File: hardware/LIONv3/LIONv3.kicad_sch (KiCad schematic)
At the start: 39 parts, among them SW1 RESET, SW2 BOOT, U1 TCAN3414DR, U14 HC-1_25-2PWT, U15 HC-1_25-2PWT, U19 HC-1_25-2PWT, U2 TYPE-C_16PIN_2MD(073), U21 USBLC6-2SC6, U3 ESP32-C6-MINI-1-N4, U4 TMP112AIDRLR, U9 HC-1_25-2PWT

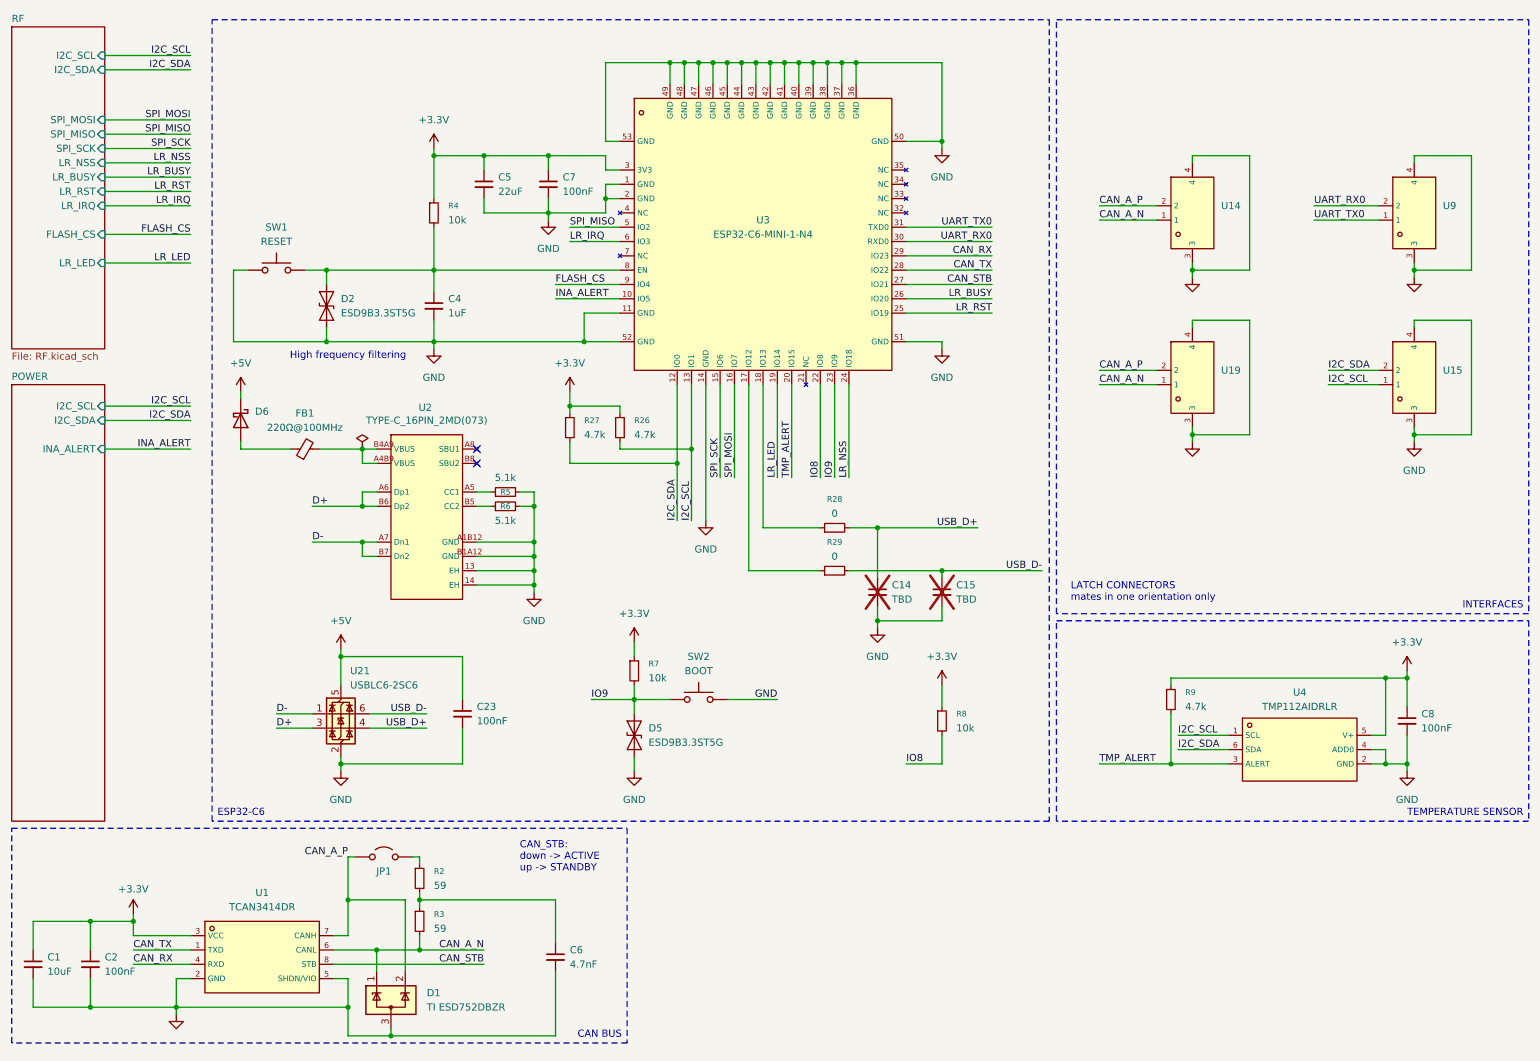
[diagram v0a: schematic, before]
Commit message: feat(hardware): change SPI terminology (new OSHWA naming conventions)
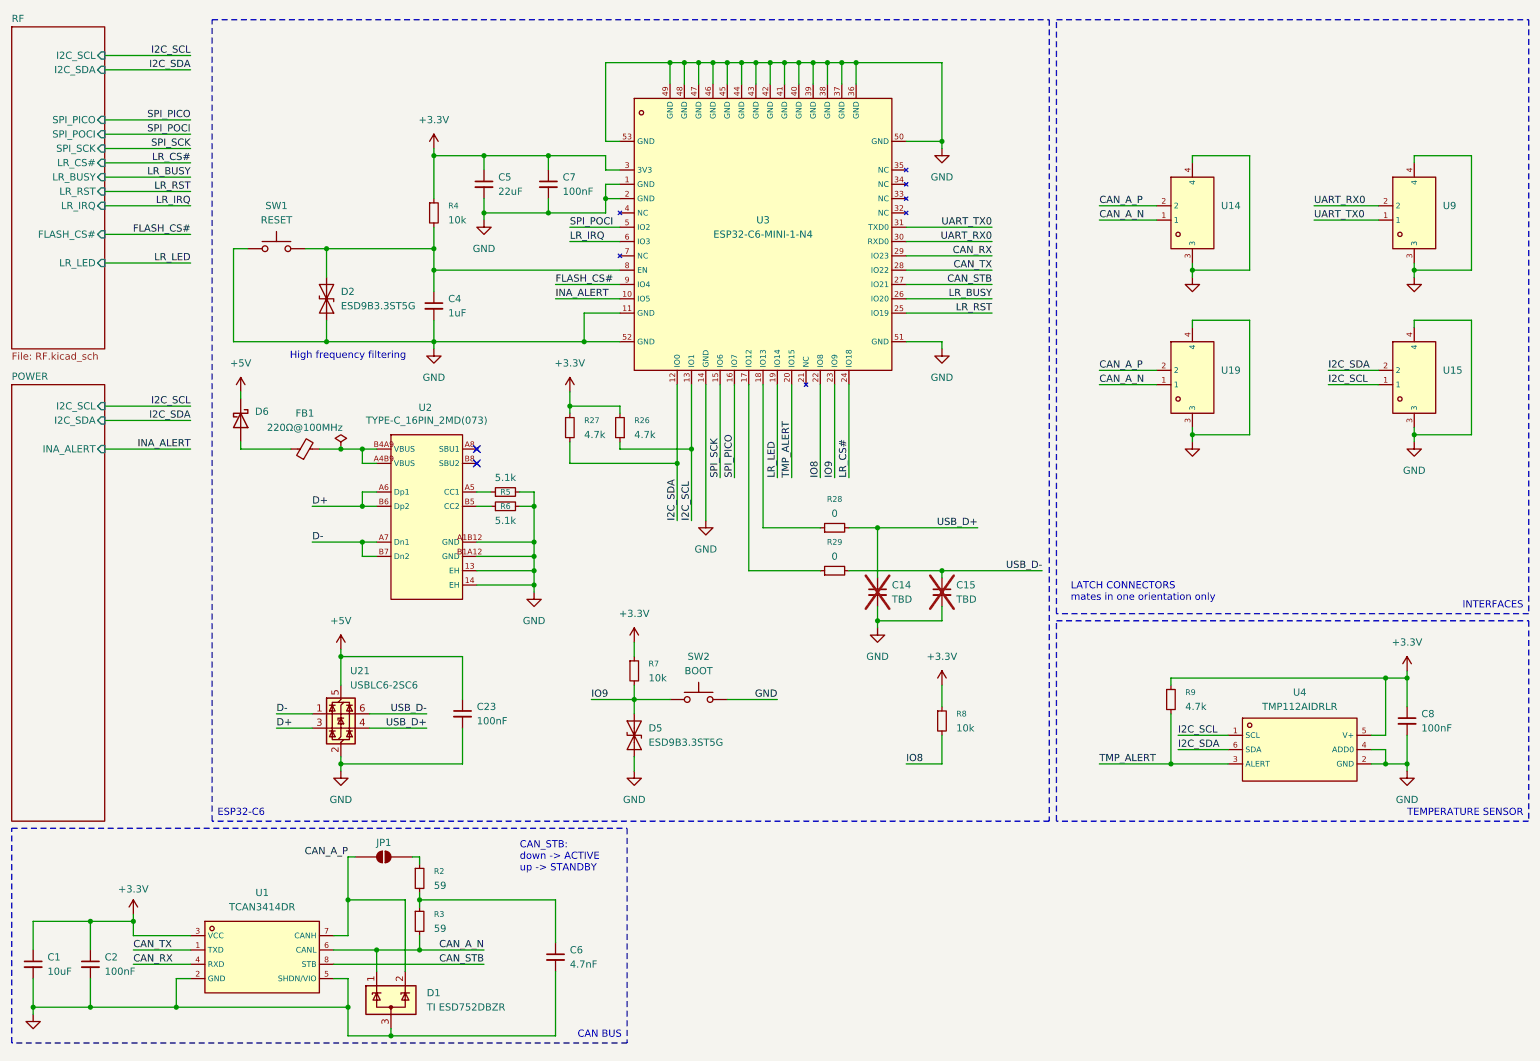
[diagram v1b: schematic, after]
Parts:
- removed JP1: Jumper_2_Open, Jumper:SolderJumper-2_P1.3mm_Open_TrianglePad1.0x1.5mm, symbol Jumper:Jumper_2_Open
- added JP1: SolderJumper_2_Open, Jumper:SolderJumper-2_P1.3mm_Open_TrianglePad1.0x1.5mm, symbol Jumper:SolderJumper_2_Open
- FB1: footprint Capacitor_SMD:C_0805_2012Metric -> Inductor_SMD:L_0805_2012Metric
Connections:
- net CAN_A_P: now also JP1.1 (A)
- net at R2.1: now also JP1.2 (B)
- net FLASH_CS renamed FLASH_CS#
- net LR_NSS renamed LR_CS#
- net SPI_MISO renamed SPI_POCI
- net SPI_MOSI renamed SPI_PICO
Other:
- sheet RF ports: added FLASH_CS#, LR_CS#, SPI_PICO, SPI_POCI; removed FLASH_CS, LR_NSS, SPI_MISO, SPI_MOSI
- moved on the sheet: D2, SW1

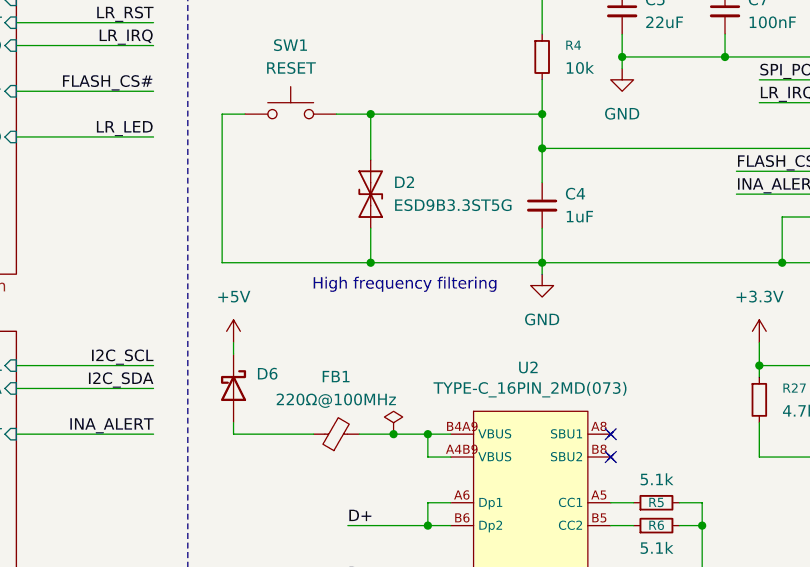
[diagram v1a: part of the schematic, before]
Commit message: feat(hardware): annotate schematic with I2C addresses
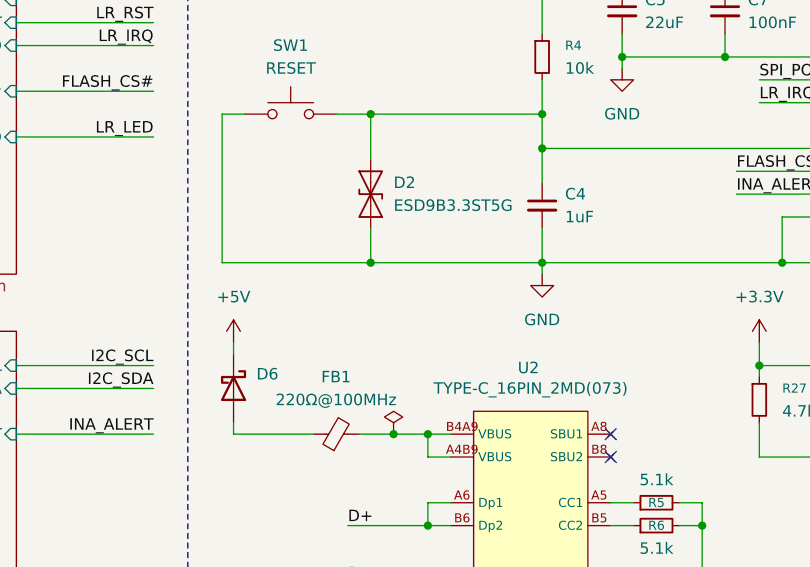
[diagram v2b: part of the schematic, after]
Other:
- note removed: "High frequency filtering"
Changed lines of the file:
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@@
 		(comment 3 "2026-08-12")
-	)
-	(text "High frequency filtering"
-		(exclude_from_sim no)
-		(at 73.66 73.66 0)
-		(effects
-			(font
-				(size 1.27 1.27)
-			)
-		)
 	)
 	(text "LATCH CONNECTORS\nmates in one orientation only"

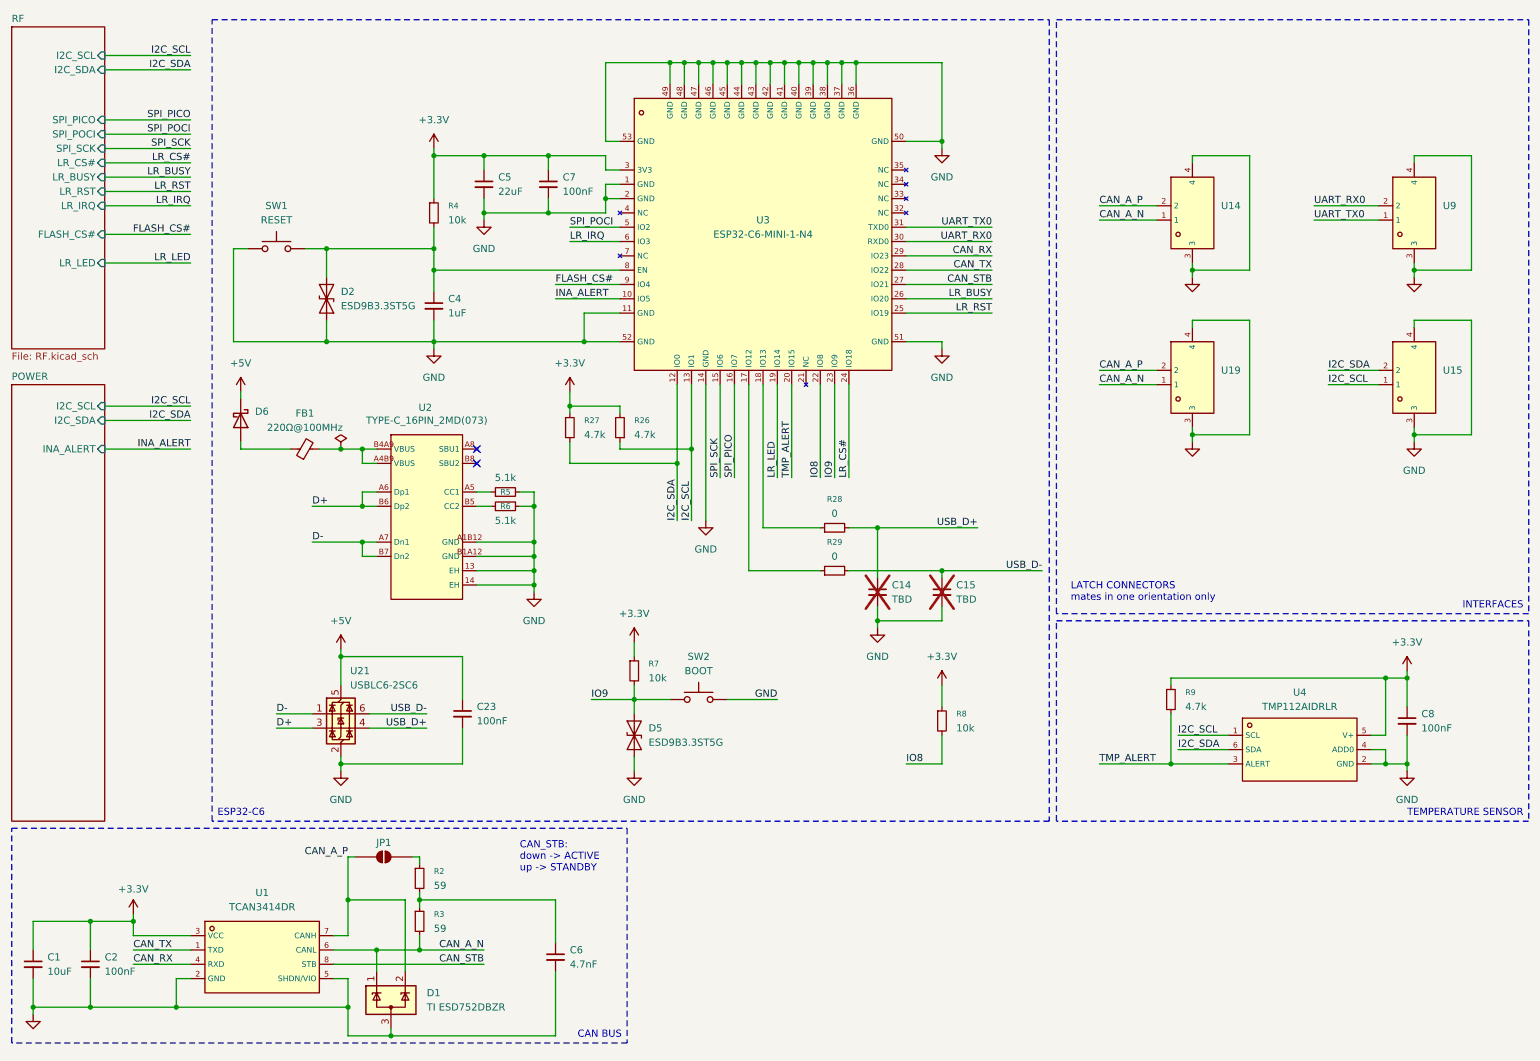
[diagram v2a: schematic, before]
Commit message: fix(hardware): fix CANbus split termination
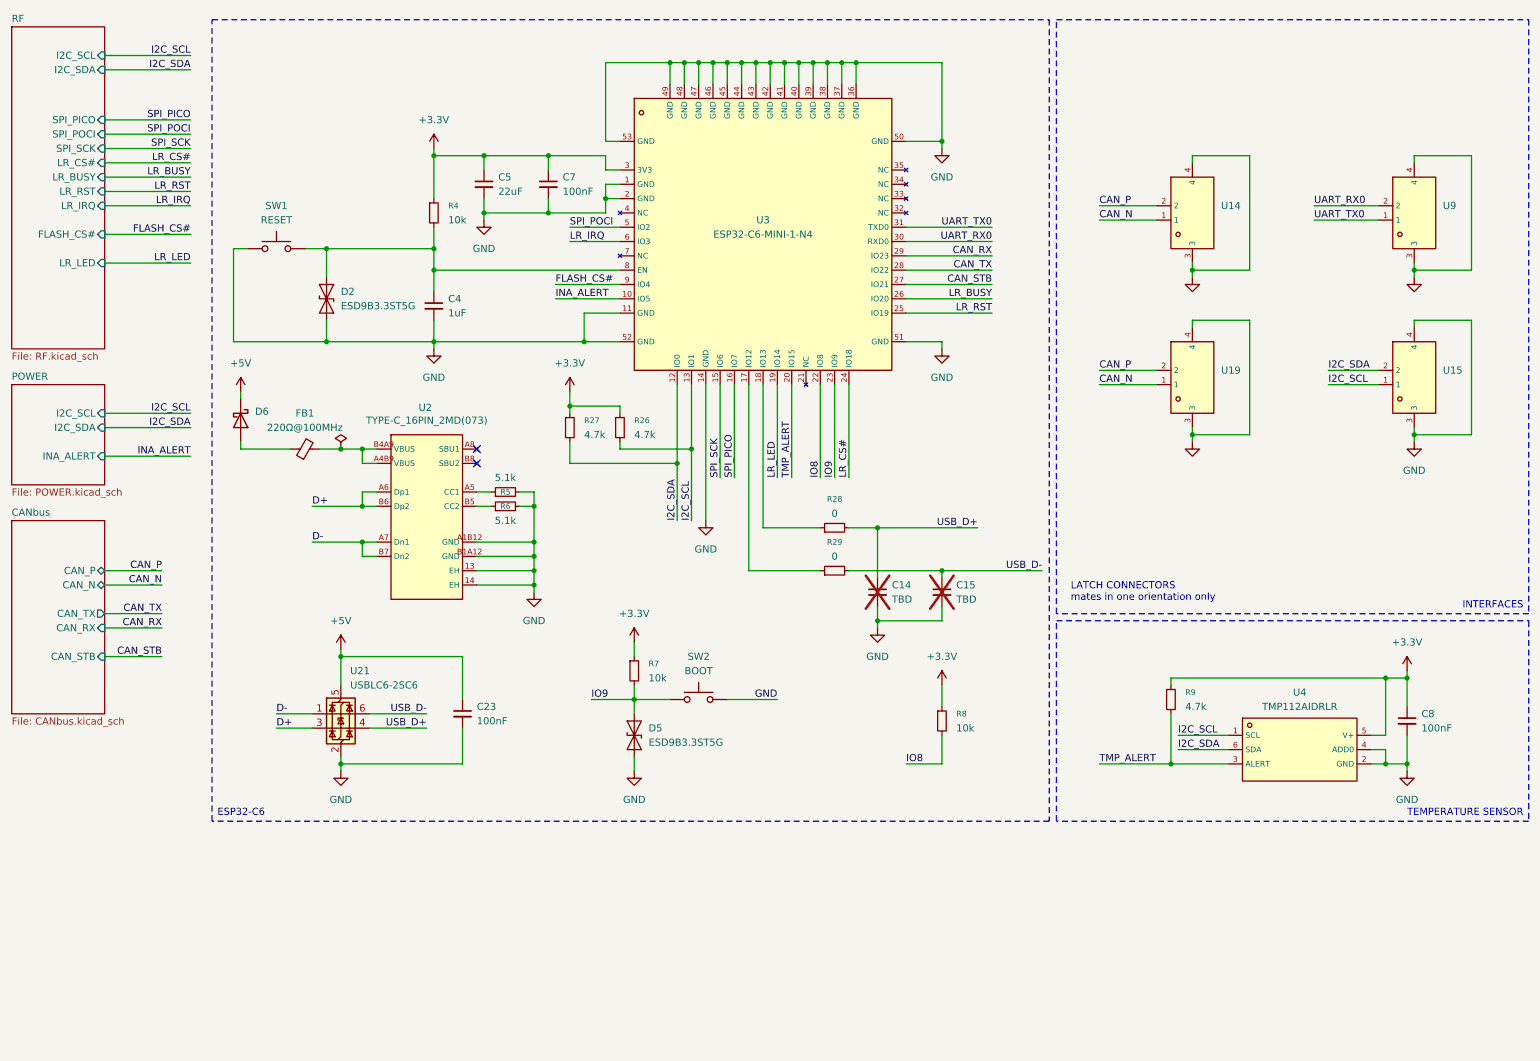
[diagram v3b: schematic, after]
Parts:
- removed C1: 10uF, Capacitor_SMD:C_0805_2012Metric, symbol Device:C_Small
- removed C2: 100nF, Capacitor_SMD:C_0402_1005Metric, symbol Device:C_Small
- removed C6: 4.7nF, Capacitor_SMD:C_0402_1005Metric, symbol Device:C_Small
- removed D1: TI ESD752DBZR, Package_TO_SOT_SMD:SOT-23-3, symbol Power_Protection:ESDA5V3L
- removed JP1: SolderJumper_2_Open, Jumper:SolderJumper-2_P1.3mm_Open_TrianglePad1.0x1.5mm, symbol Jumper:SolderJumper_2_Open
- removed R2, R3: 59, Resistor_SMD:R_0402_1005Metric, symbol Device:R_Small
- removed U1: TCAN3414DR, LIONv3-Footprints:SOIC-8_L4.9-W3.9-P1.27-LS6.0-BL, symbol LIONv3-Symbols:TCAN3414DR
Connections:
- net CAN_A_N renamed CAN_N
- net CAN_A_P renamed CAN_P
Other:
- added sheet CANbus (CANbus.kicad_sch)
- note removed: "CAN_STB: down -> ACTIVE up -> STANDBY"

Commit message: refactor(hardware): reorganize schematic
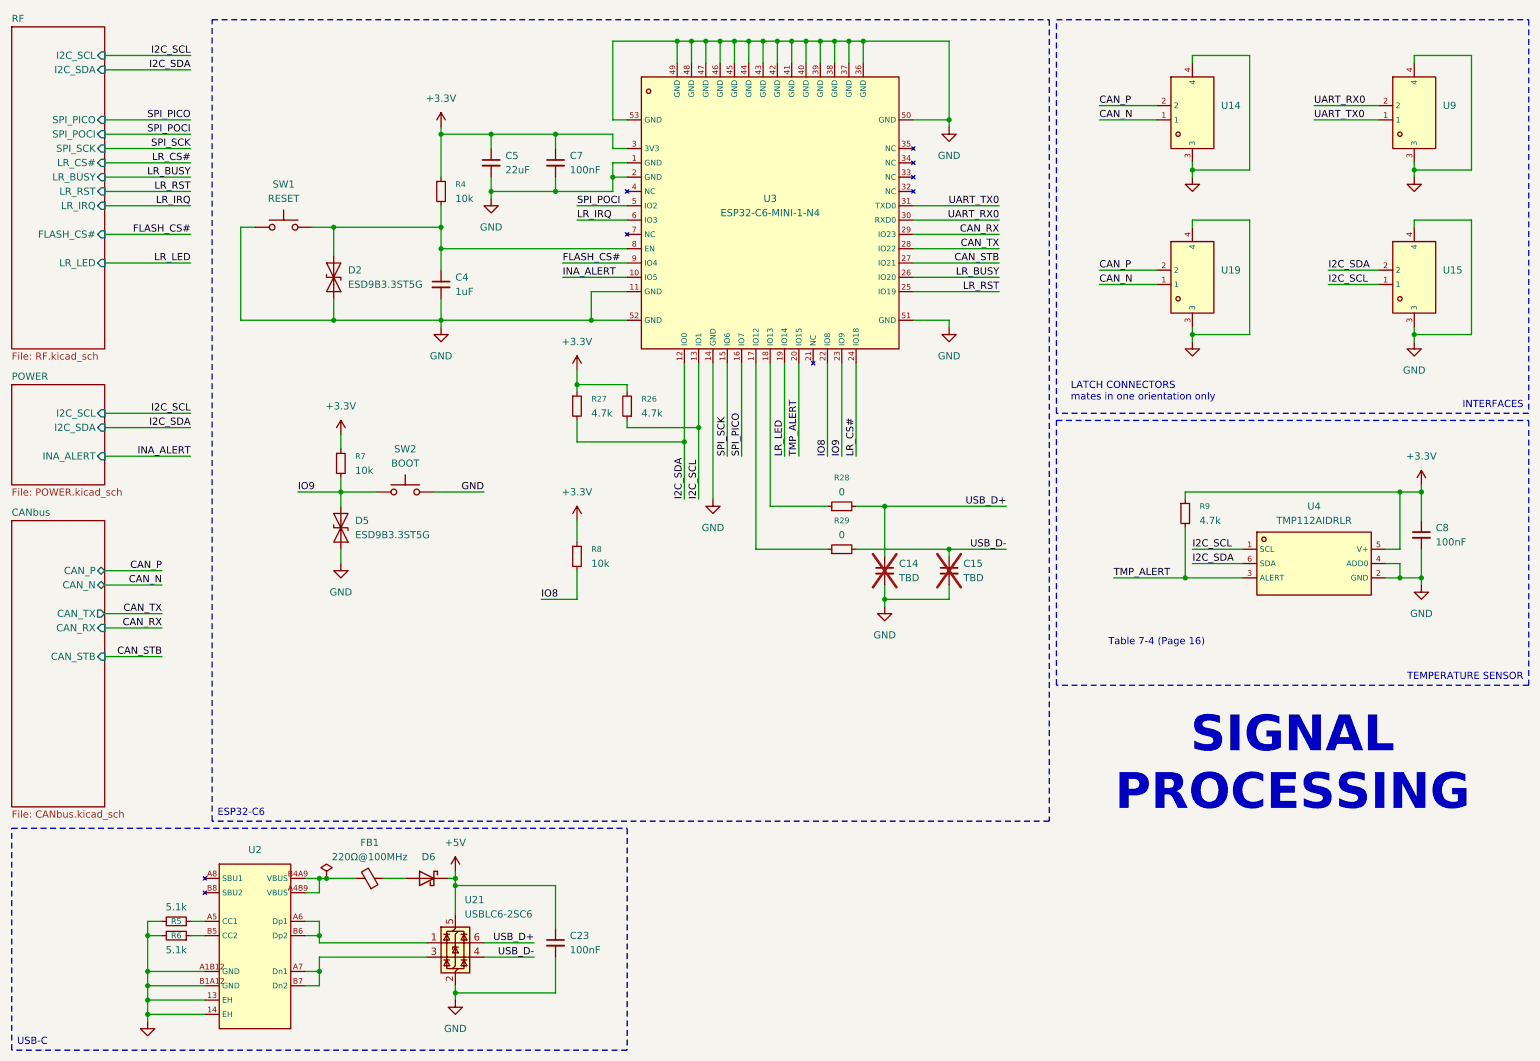
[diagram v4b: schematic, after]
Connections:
- net USB_D+: now also U21.6 (I/O1); no longer U21.4 (I/O2)
- net USB_D-: now also U21.4 (I/O2); no longer U21.6 (I/O1)
- net D+: no longer names the net of U2.A6 (Dp1), U2.B6 (Dp2)
- net D+: now also U21.1 (I/O1); no longer U21.3 (I/O2)
- net D-: no longer names the net of U2.A7 (Dn1), U2.B7 (Dn2)
- net D-: now also U21.3 (I/O2); no longer U21.1 (I/O1)
- no-connect marks 2 -> 0
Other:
- note added: "SIGNAL PROCESSING"
- note added: "Table 7-4 (Page 16)"
- moved on the sheet: C14, C15, C23, C4, C5, C7, C8, D2, D5, R26, R27, R28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

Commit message: refactor(hardware): add MPN diodes and ferrite beads
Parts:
- D6: value D_Schottky -> RB161QS-40T18R; Rating (none) -> 600mV@1A
- FB1: value 220Ω@100MHz -> BLM21PG221SN1D; Rating (none) -> 220Ω@100MHz | 2A
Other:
- note added: "BOOT CIRCUIT"
- note added: "NORMAL BOOT MODE"
- note added: "RESET CIRCUIT"
- moved on the sheet: C23, FB1, R5, R6, U2, U21
